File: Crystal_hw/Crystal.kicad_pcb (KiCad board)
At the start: 2 copper layers, 80 x 53 mm, 55 parts

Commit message: + sch v4
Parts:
- removed BN1, BN2: , BNC
- removed C23: , CAP_0805
- removed U1: , RM-8
- removed XL3: , SIL-4
- added R10: 1k, Resistors:RES_0603, F.Cu at (157.4, 97.9)
- added R11: 1k, Resistors:RES_0603, F.Cu at (192.8, 82.3)
- added R12: 1k, Resistors:RES_0603, F.Cu at (196.5, 85.6)
- added RP1: REFPOINT, PCB:REF_POINT_2MM, F.Cu at (197.1, 88.9)
- added RP2: REFPOINT, PCB:REF_POINT_2MM, F.Cu at (202.3, 86.8)
- added XW1: BNC, Connectors:BNC_R, F.Cu at (192.1, 107.4)
- added XW2: BNC, Connectors:BNC_R, F.Cu at (209.4, 107.4)
- added XW3: BNC, Connectors:BNC_R, F.Cu at (228.0, 107.6)
- C1: value (none) -> 10n; footprint RES_0603 -> Capacitors:CAP_0603
- C10, C11, C14, C4: value (none) -> 0.1u; footprint CAP_0805 -> Capacitors:CAP_0603
- C12, C19: value (none) -> 10u; footprint RES_0603 -> Capacitors:CAP_0603
- C13, C18, C5, C8: value (none) -> 0.1u; footprint RES_0603 -> Capacitors:CAP_0603
- C15: value (none) -> 1u; footprint CAP_0805 -> Capacitors:CAP_0603
- C16, C17, C20, C21: value (none) -> 1u; footprint RES_0603 -> Capacitors:CAP_0603
- C2, C7, C9: value (none) -> 10u; footprint CAP_0805 -> Capacitors:CAP_0603
- C22: value (none) -> 10n; footprint CAP_0805 -> Capacitors:CAP_0603
- C3: value (none) -> 18pF; footprint CAP_0805 -> Capacitors:CAP_0603
- C6: value (none) -> 18pF; footprint RES_0603 -> Capacitors:CAP_0603
- D1, D2, D3: value (none) -> LED; footprint LED-5MM -> LEDs:LED_0603
- DA1: value (none) -> MAX4453; footprint SOT23-8 -> SOT:SOT23-8
- DA2: value (none) -> ADS8320; footprint RM-8 -> SO_DIL_TSSOP:MSOP8
- DA3: value (none) -> DAC8531; footprint RM-8 -> SO_DIL_TSSOP:MSOP8
- DA4, DA5: value (none) -> MCP1700; footprint SOT223 -> SOT:SOT23-3A
- DD1: value (none) -> STM32F405RX-64; footprint LQFP64 -> LQFP_TQFP:LQFP64
- HOLE1, HOLE2, HOLE3, HOLE4: value (none) -> HOLE_METALLED; footprint Hole3_5_out6mm -> PCB:Hole3_5_out6mm
- R1: value (none) -> 1M; footprint RES_0603 -> Resistors:RES_0603
- R2, R3, R7: value (none) -> 10k; footprint RES_0603 -> Resistors:RES_0603
- R4, R9: value (none) -> 1k; footprint RES_0603 -> Resistors:RES_0603
- R5, R6: value (none) -> 10K; footprint RES_0603 -> Resistors:RES_0603
- R8: value (none) -> 5R1; footprint RES_0603 -> Resistors:RES_0603
- SW1: value (none) -> BUTTON_H; footprint BUTTON_6x6SMD -> BtnsSwitches:BTN_4x4_SMD
- VCap1, VCap2: value (none) -> 2.2u; footprint RES_0603 -> Capacitors:CAP_0603
- XL1: value (none) -> CONN_6; footprint SIL-3 -> Connectors:PLS-6
- XL2: value (none) -> USB_MINI_B; footprint USBmicro_MOLEX_WM17142 -> Connectors:USBmicro_MOLEX_WM17142
- XTAL1: value (none) -> 12 MHz; footprint CRYSTAL_0503x4-4 -> Quartz:03225C4
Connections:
- C1 pad 1: GND -> Net-(C1-Pad1)
- C1 pad 2: N-0000067 -> GND
- C10 pad 1: GND -> +3.3V
- C10 pad 2: +5V -> GND
- C11 pad 1: GND -> +3.3V
- C11 pad 2: +3.3V -> GND
- C12 pad 1: N-0000070 -> VAA
- C13 pad 1: N-0000069 -> +3.3V
- C14 pad 1: GND -> Net-(C14-Pad1)
- C14 pad 2: +5V -> GND
- C15 pad 1: GND -> Net-(C14-Pad1)
- C15 pad 2: VAA -> GND
- C16 pad 1: +3.3V -> +5V
- C17 pad 1: +3.3V -> +5V
- C18 pad 1: +3.3V -> GND
- C18 pad 2: GND -> VAA
- C19 pad 1: +3.3V -> GND
- C19 pad 2: GND -> VAA
- C2 pad 1: N-0000067 -> +3.3V
- C21 pad 1: +3.3V -> VAA
- C22 pad 1: +3.3V -> +5V
- C3 pad 1: GND -> Net-(C3-Pad1)
- C3 pad 2: VAA -> GND
- C4 pad 1: GND -> +3.3V
- C4 pad 2: N-0000015 -> GND
- C5 pad 1: /D2 -> +3.3V
- C6 pad 1: +3.3V -> Net-(C6-Pad1)
- C7 pad 1: N-000006 -> GND
- C7 pad 2: N-000008 -> Net-(C7-Pad2)
- C8 pad 1: GND -> +3.3V
- C8 pad 2: VAA -> GND
- C9 pad 1: GND -> Net-(C9-Pad1)
- C9 pad 2: VAA -> Net-(C9-Pad2)
- D1 pad A: N-0000066 -> Net-(D1-PadA)
- D2 pad A: N-0000019 -> Net-(D2-PadA)
- D3 pad A: N-0000068 -> Net-(D3-PadA)
- DA1 pad 3: N-0000015 -> Net-(C7-Pad2)
- DA1 pad 6: N-000008 -> Net-(DA1-Pad6)
- DA1 pad 7: N-000008 -> Net-(DA1-Pad7)
- DA2 pad 1: VAA -> Net-(C14-Pad1)
- DA2 pad 2: VAA -> Net-(DA1-Pad7)
- DA2 pad 3: /S1 -> GND
- DA2 pad 4: /S1 -> GND
- DA2 pad 5: /CS -> /ADC_CS
- DA2 pad 6: /CLK -> /ADC_DOUT
- DA2 pad 7: /DIN -> /ADC_CLK
- DA2 pad 8: GND -> Net-(C14-Pad1)
- DA3 pad 2: N-000008 -> VAA
- DA3 pad 3: GND -> Net-(DA3-Pad3)
- DA3 pad 4: GND -> Net-(DA3-Pad3)
- DA3 pad 5: /CSIN -> /DAC_CS
- DA3 pad 6: /DOUT -> /DAC_CLK
- DA3 pad 7: /SCK -> /DAC_DIN
- DA3 pad 8: N-0000067 -> GND
- DD1 pad 20: /CSIN -> /ADC_CS
- DD1 pad 21: /SCK -> /ADC_CLK
- DD1 pad 22: /DOUT -> /ADC_DOUT
- DD1 pad 33: /CS -> /DAC_CS
- DD1 pad 34: /CLK -> /DAC_CLK
- DD1 pad 36: /DIN -> /DAC_DIN
- DD1 pad 37: N-0000042 -> Net-(DD1-Pad37)
- DD1 pad 38: N-0000065 -> Net-(DD1-Pad38)
- DD1 pad 39: N-0000018 -> Net-(DD1-Pad39)
- DD1 pad 42: /TX1 -> /UART_TX
- DD1 pad 43: /RX1 -> /UART_RX
- DD1 pad 5: N-0000070 -> Net-(C3-Pad1)
- DD1 pad 6: N-0000013 -> Net-(DD1-Pad6)
- DD1 pad 60: N-0000016 -> Net-(DD1-Pad60)
- DD1 pad 8: /IN1 -> (no net)
- DD1 pad 9: /IN2 -> (no net)
- R1 pad 1: N-0000067 -> Net-(C1-Pad1)
- R1 pad 2: VAA -> GND
- R2 pad 2: N-0000015 -> Net-(C7-Pad2)
- R3 pad 1: /S1 -> Net-(C7-Pad2)
- R3 pad 2: /S2_D1 -> GND
- R4 pad 1: N-0000015 -> Net-(DD1-Pad6)
- R4 pad 2: GND -> Net-(C6-Pad1)
- R5 pad 1: N-0000013 -> Net-(DA1-Pad6)
- R5 pad 2: N-0000069 -> Net-(C9-Pad2)
- R6 pad 1: N-0000042 -> Net-(DA1-Pad7)
- R6 pad 2: N-0000066 -> Net-(DA1-Pad6)
- R7 pad 1: N-0000065 -> Net-(DD1-Pad60)
- R7 pad 2: N-0000019 -> GND
- R8 pad 1: N-0000018 -> VAA
- R8 pad 2: N-0000068 -> Net-(C14-Pad1)
- R9 pad 1: N-0000016 -> Net-(DD1-Pad37)
- R9 pad 2: GND -> Net-(D1-PadA)
- SW1 pad 1: N-0000016 -> Net-(DD1-Pad60)
- XL1 pad 1: /RX1 -> +3.3V
- XL1 pad 2: /TX1 -> /SWCLK
- XTAL1 pad 1: N-0000070 -> Net-(C3-Pad1)
- XTAL1 pad 2: N-0000069 -> Net-(C6-Pad1)
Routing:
- net (no net): track 0.00 -> 116.6 mm, vias 0 -> 4
- net N-0000018: track 94.8 -> 0.00 mm
- net N-0000065: track 89.6 -> 0.00 mm, vias 2 -> 0
- net N-0000042: track 85.2 -> 0.00 mm, vias 2 -> 0
- net Net-(DD1-Pad60): track 0.00 -> 83.1 mm, vias 0 -> 2
- net VAA: track 114.7 -> 190.0 mm
- net /IN2: track 60.3 -> 0.00 mm, vias 2 -> 0
- net /IN1: track 56.2 -> 0.00 mm, vias 2 -> 0
- net Net-(C1-Pad1): track 0.00 -> 36.1 mm, vias 0 -> 1
- net /UART_RX: track 0.00 -> 22.4 mm
- net /RX1: track 22.4 -> 0.00 mm
- net +3.3V: track 198.4 -> 176.4 mm
- net /S2_D1: track 18.3 -> 0.00 mm
- net /CLK: track 70.5 -> 58.5 mm
- net /CS: track 71.0 -> 59.7 mm
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
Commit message: HW v20190412 in progress
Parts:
- added L1: 90R, Inductors:DLW21SN, F.Cu at (143.0, 90.0)
- added L2: BLM15AG102, Inductors:IND_0402, F.Cu at (120.8, 119.6)
- added R13: 2R0, Resistors:RES_0603, F.Cu at (146.6, 84.8)
- added R14: 10K, Resistors:RES_0603, F.Cu at (114.8, 125.0)
- added TP1: TESTPOINT, PCB:TESTPOINT_1MM, F.Cu at (97.6, 125.0)
- added TP10: TESTPOINT, PCB:TESTPOINT_1MM, F.Cu at (134.0, 129.0)
- added TP11: TESTPOINT, PCB:TESTPOINT_1MM, F.Cu at (132.0, 129.0)
- added TP12: TESTPOINT, PCB:TESTPOINT_1MM, F.Cu at (139.0, 125.0)
- added TP13: TESTPOINT, PCB:TESTPOINT_1MM, F.Cu at (128.2, 92.0)
- added TP14: TESTPOINT, PCB:TESTPOINT_1MM, F.Cu at (108.2, 113.6)
- added TP2: TESTPOINT, PCB:TESTPOINT_1MM, F.Cu at (106.4, 125.0)
- added TP3: TESTPOINT, PCB:TESTPOINT_1MM, F.Cu at (111.4, 119.0)
- added TP4: TESTPOINT, PCB:TESTPOINT_1MM, F.Cu at (112.0, 125.0)
- added TP5: TESTPOINT, PCB:TESTPOINT_1MM, F.Cu at (118.4, 119.6)
- added TP6: TESTPOINT, PCB:TESTPOINT_1MM, F.Cu at (123.4, 129.0)
- added TP7: TESTPOINT, PCB:TESTPOINT_1MM, F.Cu at (119.4, 129.0)
- added TP8: TESTPOINT, PCB:TESTPOINT_1MM, F.Cu at (121.4, 129.0)
- added TP9: TESTPOINT, PCB:TESTPOINT_1MM, F.Cu at (136.0, 129.0)
- added U1: USBLC6, SOT:SOT23-6, F.Cu at (143.0, 85.0)
- added XL3: CONN_1, Connectors:PLS-1Rnd, F.Cu at (137.0, 105.0)
- added XL4: CONN_1, Connectors:PLS-1Rnd, F.Cu at (143.0, 137.0)
- C12, C7: value 10u -> 1u
- C22: value 10n -> 2u2
- RP1, RP2: footprint PCB:REF_POINT_2MM -> PCB:REF_POINT_1MM
- XL2: value USB_MINI_B -> USB_MICRO; footprint Connectors:USBmicro_MOLEX_WM17142 -> Connectors:USBmicro_MOLEX_1050170001
- XW1, XW2, XW3: footprint Connectors:BNC_R -> Connectors:BNC2
- moved HOLE1 153.1 mm to (88.0, 80.0)
- moved D3 143.4 mm to (102.2, 93.0), turned to 180 degrees
- moved D2 142.8 mm to (102.2, 89.0), turned to 180 degrees
- moved D1 142.1 mm to (102.2, 85.0), turned to 180 degrees
- moved R9 127.1 mm to (123.6, 87.4), turned to 180 degrees
- moved C9 126.0 mm to (100.6, 125.0), turned to 0 degrees
- moved SW1 124.3 mm to (122.2, 80.0)
- moved R6 123.3 mm to (109.2, 125.0), turned to 180 degrees
- moved R3 120.7 mm to (106.0, 117.0), turned to 90 degrees
- moved XW2 120.7 mm to (90.0, 125.0), turned to 180 degrees
- moved R7 115.3 mm to (125.0, 94.0), turned to 90 degrees
- moved RP2 109.6 mm to (93.0, 78.0)
- moved R8 109.0 mm to (125.2, 122.2), turned to 180 degrees
- moved C8 107.9 mm to (123.0, 94.0), turned to 90 degrees
- moved XW1 103.7 mm to (90.0, 89.0), turned to 180 degrees
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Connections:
- net +3.3V renamed +3v3
- C15 pad 1: Net-(C14-Pad1) -> Net-(C15-Pad1)
- C16 pad 1: +5V -> +5v
- C17 pad 1: +5V -> +5v
- C22 pad 1: +5V -> Net-(C22-Pad1)
- DA2 pad 2: Net-(DA1-Pad7) -> Net-(DA2-Pad2)
- DA2 pad 8: Net-(C14-Pad1) -> Net-(C15-Pad1)
- DA4 pad 3: +5V -> +5v
- DA5 pad 3: +5V -> +5v
- DD1 pad 20: /ADC_CS -> (no net)
- DD1 pad 23: (no net) -> /ADC_CS
- DD1 pad 37: Net-(DD1-Pad37) -> (no net)
- DD1 pad 38: Net-(DD1-Pad38) -> (no net)
- DD1 pad 39: Net-(DD1-Pad39) -> (no net)
- DD1 pad 41: (no net) -> Net-(DD1-Pad41)
- DD1 pad 58: (no net) -> Net-(DD1-Pad58)
- DD1 pad 59: (no net) -> Net-(DD1-Pad59)
- DD1 pad 61: (no net) -> Net-(DD1-Pad61)
- R10 pad 1: Net-(DD1-Pad38) -> Net-(DD1-Pad59)
- R11 pad 1: Net-(DD1-Pad39) -> Net-(DD1-Pad61)
- R8 pad 2: Net-(C14-Pad1) -> Net-(C15-Pad1)
- R9 pad 1: Net-(DD1-Pad37) -> Net-(DD1-Pad58)
- XL2 pad 1: +5V -> +5v
- XL2 pad 2: /DM -> Net-(U1-Pad1)
- XL2 pad 3: /DP -> Net-(U1-Pad3)
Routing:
- net GND: track 802.5 -> 369.4 mm, vias 77 -> 198
- net VAA: track 190.0 -> 54.7 mm, vias 6 -> 3
- net (no net): track 116.6 -> 0.00 mm, vias 4 -> 0
- net +5V: track 104.1 -> 0.00 mm, vias 3 -> 0
- net N-0000016: track 75.4 -> 0.00 mm
- net /DIN: track 63.2 -> 0.00 mm, vias 2 -> 0
- net /CS: track 59.7 -> 0.00 mm, vias 2 -> 0
- net +3v3: track 176.4 -> 117.4 mm, vias 10 -> 7
- net /CLK: track 58.5 -> 0.00 mm, vias 2 -> 0
- net +5v: track 0.00 -> 56.7 mm, vias 0 -> 3
- net Net-(DD1-Pad60): track 83.1 -> 28.4 mm
- net Net-(C9-Pad1): track 0.00 -> 45.8 mm
- net /DAC_DIN: track 0.00 -> 28.2 mm
- net /DAC_CLK: track 0.00 -> 27.0 mm
- net /DAC_CS: track 0.00 -> 25.7 mm
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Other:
- board size 80 x 53 mm -> 72 x 63 mm
- net class Default: trace_width 0.254 -> 0.2; via_dia 0.889 -> 0.7; via_drill 0.635 -> 0.3
- net class Wide added: clearance 0.2, trace_width 0.5, via_dia 0.7, via_drill 0.3
- rule pad_to_mask_clearance: 0.1 -> 0.06
- rule via_min_drill: 0.4 -> 0.3
- rule via_min_size: 0.889 -> 0.4

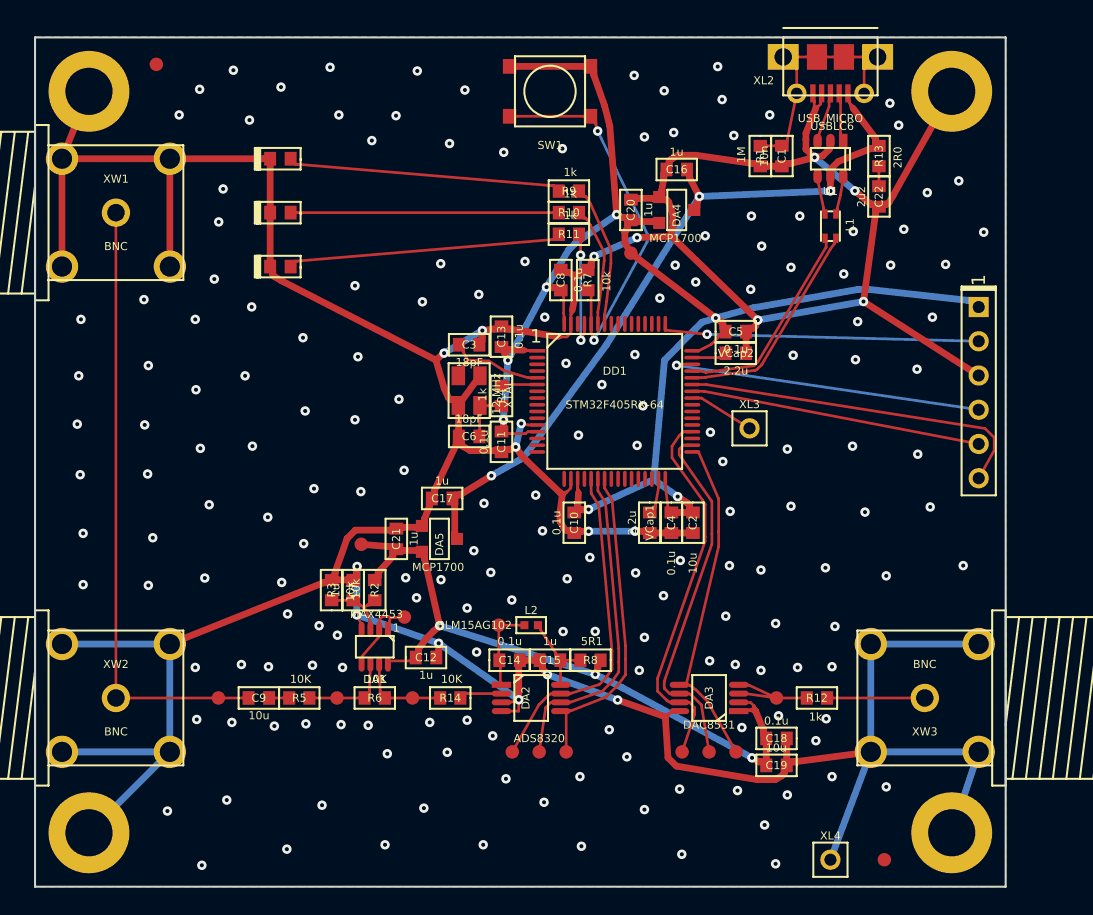
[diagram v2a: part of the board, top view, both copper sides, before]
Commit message: switching to newer framework
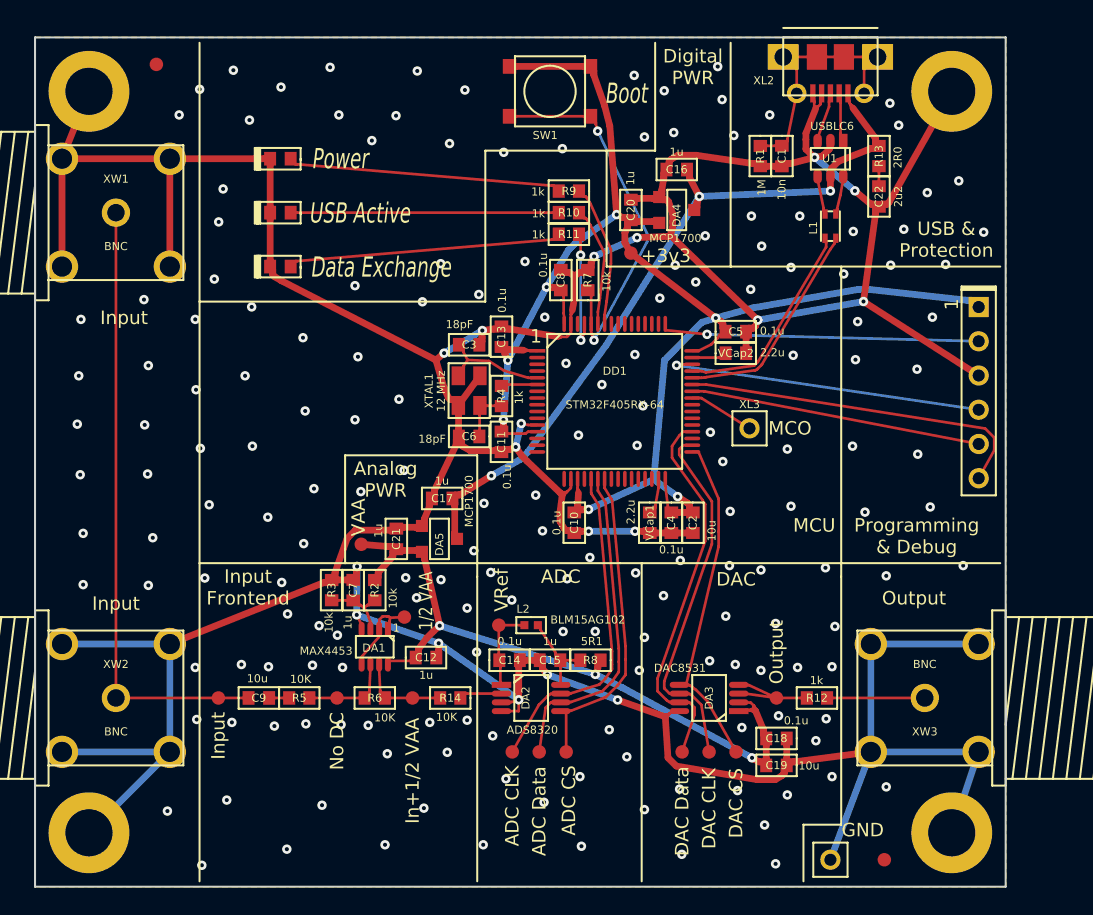
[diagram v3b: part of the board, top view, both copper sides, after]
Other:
- board text added: "+3v3"
- board text added: "1/2 VAA"
- board text added: "ADC"
- board text added: "ADC CLK"
- board text added: "ADC CS"
- board text added: "ADC Data"
- board text added: "Analog PWR"
- board text added: "Boot"
- board text added: "DAC"
- board text added: "DAC CLK"
- board text added: "DAC CS"
- board text added: "DAC Data"
- board text added: "Data Exchange"
- board text added: "Digital PWR"
- board text added: "GND"
- board text added: "In+1/2 VAA"
- board text added: "Input"
- board text added: "Input Frontend"
- board text added: "MCO"
- board text added: "MCU"
- board text added: "No DC"
- board text added: "Output"
- board text added: "Power"
- board text added: "Programming & Debug"
- board text added: "USB & Protection"
- board text added: "USB Active"
- board text added: "VAA"
- board text added: "VRef"
